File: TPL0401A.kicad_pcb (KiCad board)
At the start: 2 copper layers, 19.9 x 12.4 mm, 4 parts, among them J1 Conn_01x04_Male, J2 Conn_01x04_Male, U1 TPL0401A-10-Q1

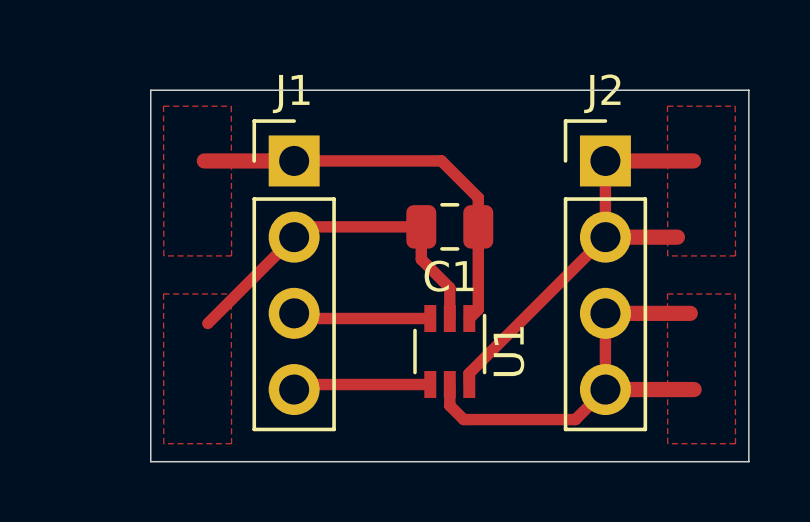
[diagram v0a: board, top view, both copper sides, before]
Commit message: TPL0401A: Pull up SCL and SDA in PCB
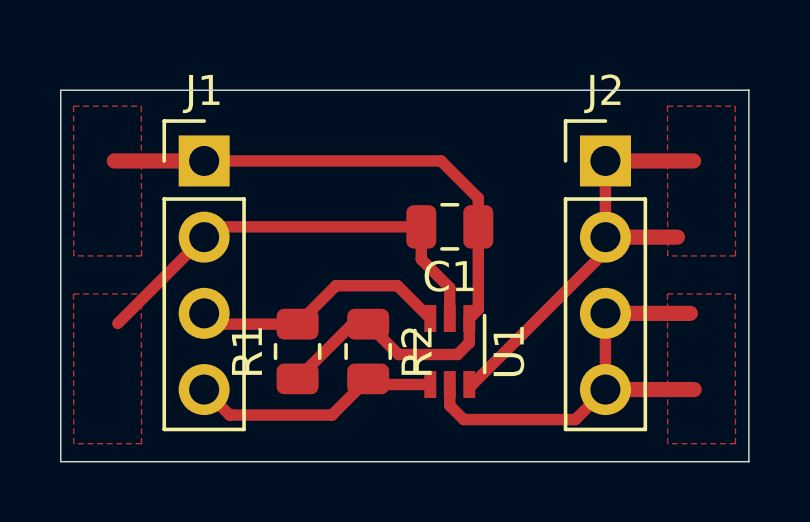
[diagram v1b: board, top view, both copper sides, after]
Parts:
- added R1: R, Resistor_SMD:R_0805_2012Metric, F.Cu at (147.9, 112.9)
- added R2: R, Resistor_SMD:R_0805_2012Metric, F.Cu at (150.2, 112.9)
- moved J1 3.00 mm to (144.7, 106.5)
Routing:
- net +5V: track 13.8 -> 24.7 mm
- net SCL: track 4.61 -> 8.91 mm
- net SDA: track 4.61 -> 8.70 mm
- net GND: track 11.9 -> 14.9 mm
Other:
- board size 19.9 x 12.4 mm -> 22.9 x 12.4 mm
